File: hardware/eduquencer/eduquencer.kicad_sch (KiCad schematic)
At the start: 5 parts, among them J1 AudioJack2_SwitchT, J2 AudioJack2_SwitchT, U1 Pico

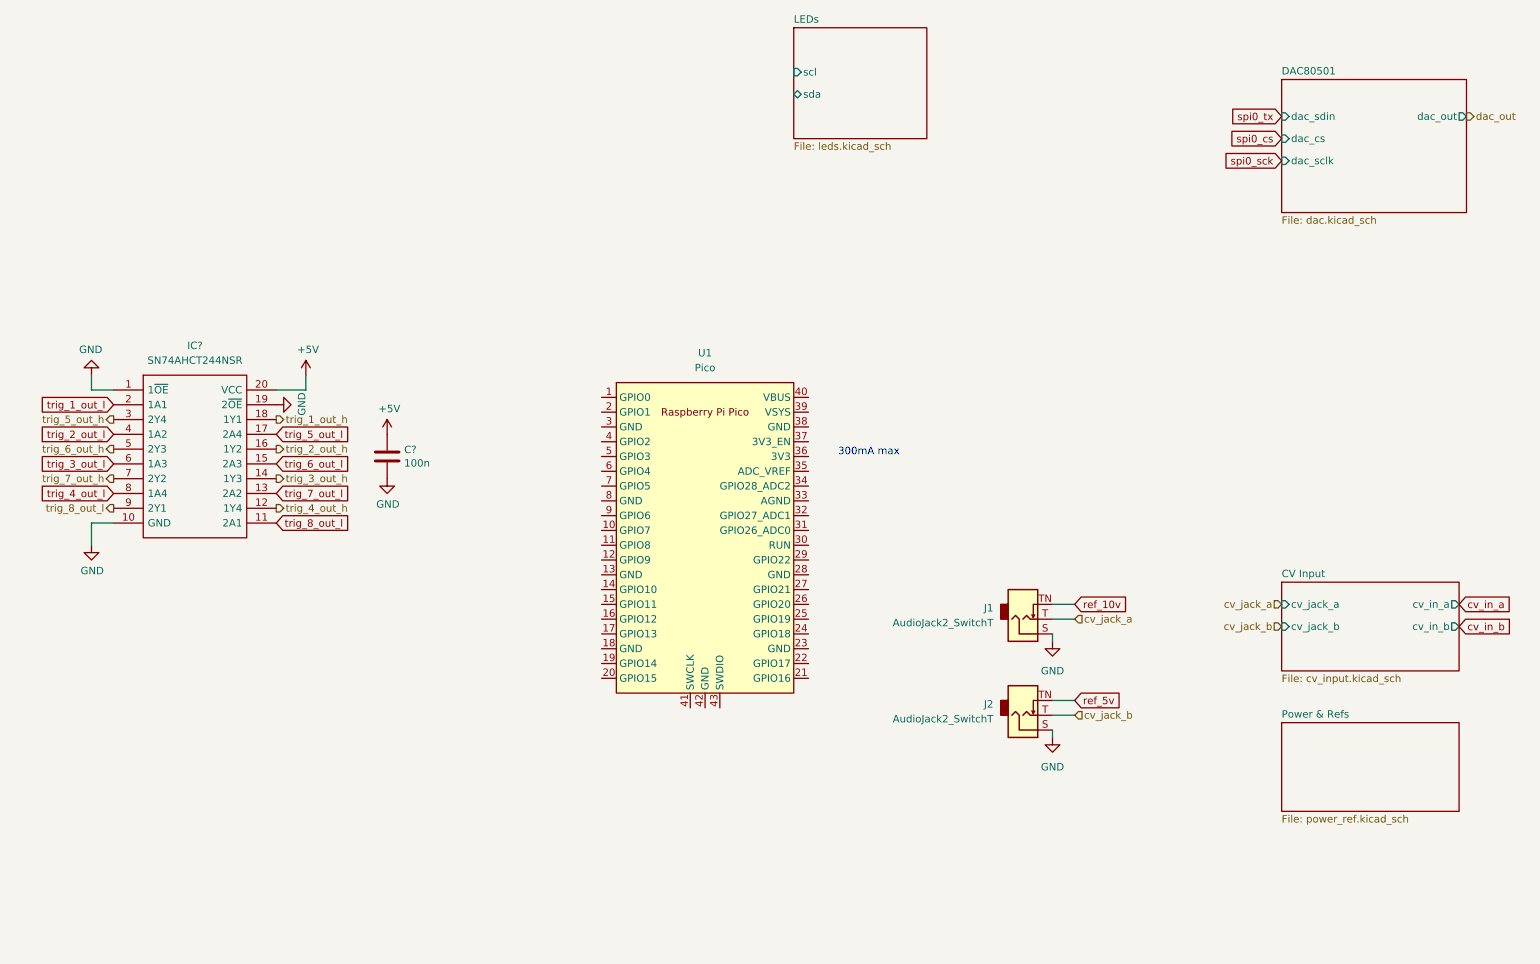
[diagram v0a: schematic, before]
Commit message: Hardware: add button sheet
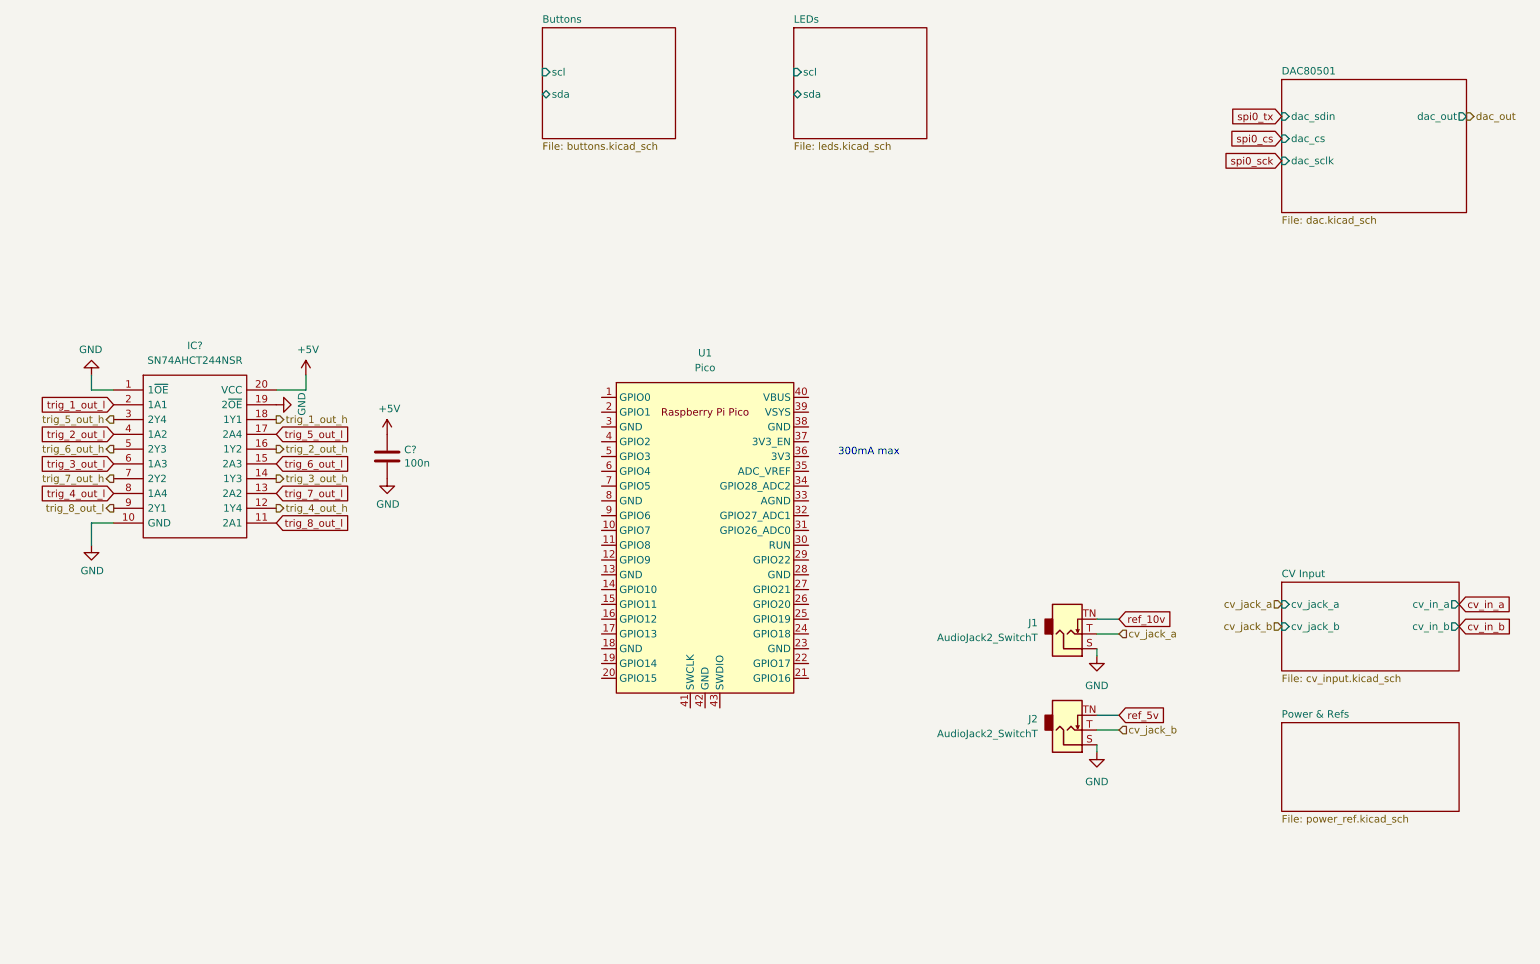
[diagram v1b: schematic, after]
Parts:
- J1, J2: footprint (none) -> AudioJacks:Jack_3.5mm_QingPu_WQP-PJ301BM_Vertical
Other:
- added sheet Buttons (buttons.kicad_sch)
- moved on the sheet: J1, J2

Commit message: Hardware: add trigger in&outputs, wire rpi
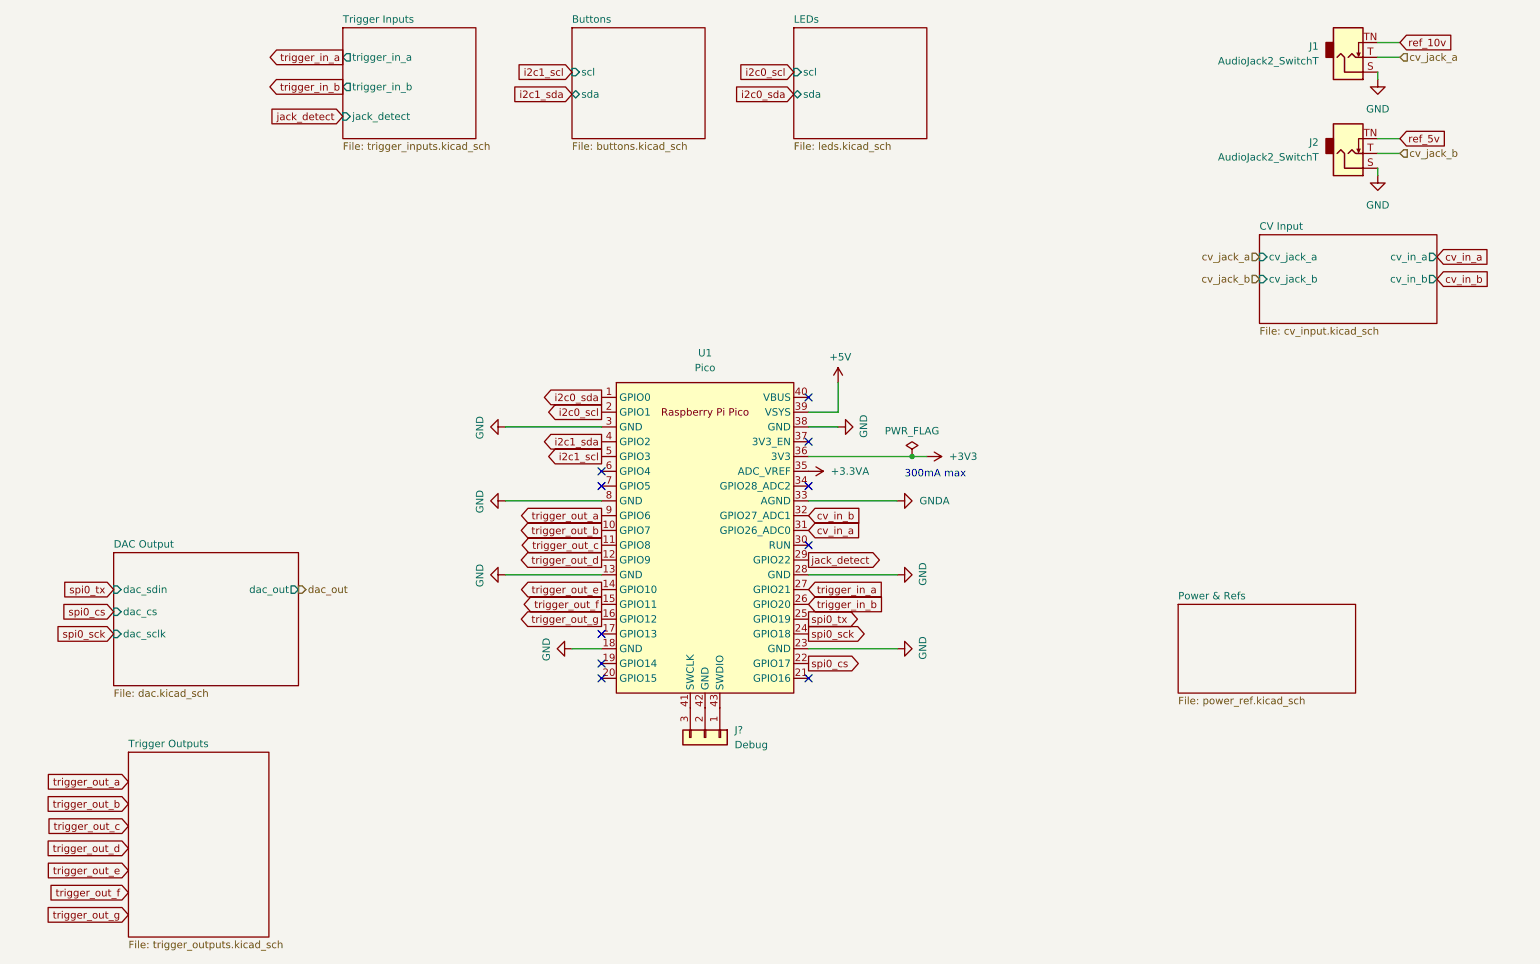
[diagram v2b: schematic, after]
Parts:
- removed C?: 100n, Capacitor_SMD:C_0603_1608Metric, symbol Device:C
- removed IC?: SN74AHCT244NSR, SOIC127P780X200-20N, symbol SN74AHCT244NSR:SN74AHCT244NSR
- added J?: Debug, symbol Connector_Generic:Conn_01x03
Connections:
- net +5V: now also U1.39 (VSYS)
- net GND: now also U1.13 (GND), U1.18 (GND), U1.23 (GND), U1.28 (GND), U1.3 (GND), U1.38 (GND), U1.8 (GND)
- net cv_in_a: now also U1.31 (GPIO26_ADC0)
- net cv_in_b: now also U1.32 (GPIO27_ADC1)
- net spi0_cs: now also U1.22 (GPIO17)
- net spi0_sck: now also U1.24 (GPIO18)
- net spi0_tx: now also U1.25 (GPIO19)
- net i2c0_sda: now reaches U1.1 (GPIO0)
- net trigger_out_b: now reaches U1.10 (GPIO7)
- net trigger_out_c: now reaches U1.11 (GPIO8)
- net trigger_out_d: now reaches U1.12 (GPIO9)
- net trigger_out_e: now reaches U1.14 (GPIO10)
- net trigger_out_f: now reaches U1.15 (GPIO11)
- net trigger_out_g: now reaches U1.16 (GPIO12)
- net i2c0_scl: now reaches U1.2 (GPIO1)
- net trigger_in_b: now reaches U1.26 (GPIO20)
- net trigger_in_a: now reaches U1.27 (GPIO21)
- net jack_detect: now reaches U1.29 (GPIO22)
- net GNDA: now reaches U1.33 (AGND)
- net +3.3VA: now reaches U1.35 (ADC_VREF)
- net +3V3: now reaches U1.36 (3V3)
- net i2c1_sda: now reaches U1.4 (GPIO2)
- net at U1.41 (SWCLK): now also J?.3 (Pin_3)
- net at U1.42 (GND): now also J?.2 (Pin_2)
- net at U1.43 (SWDIO): now also J?.1 (Pin_1)
- net i2c1_scl: now reaches U1.5 (GPIO3)
- net trigger_out_a: now reaches U1.9 (GPIO6)
- no-connect marks 0 -> 10
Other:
- sheet DAC80501 renamed DAC Output
- added sheet Trigger Inputs (trigger_inputs.kicad_sch)
- added sheet Trigger Outputs (trigger_outputs.kicad_sch)
- moved on the sheet: J1, J2

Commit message: Hardware: add test points, tiny cleanup
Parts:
- removed J1, J2: AudioJack2_SwitchT, AudioJacks:Jack_3.5mm_QingPu_WQP-PJ301BM_Vertical, symbol Connector:AudioJack2_SwitchT
- added TP?: SPI0 TX, TestPoint:TestPoint_Pad_2.0x2.0mm, symbol Connector:TestPoint
- added TP?: SPI0 CS, TestPoint:TestPoint_Pad_2.0x2.0mm, symbol Connector:TestPoint
- added TP?: I2C0 SDA, TestPoint:TestPoint_Pad_2.0x2.0mm, symbol Connector:TestPoint
- added TP?: I2C1 SCL, TestPoint:TestPoint_Pad_2.0x2.0mm, symbol Connector:TestPoint
- added TP?: I2C1 SDA, TestPoint:TestPoint_Pad_2.0x2.0mm, symbol Connector:TestPoint
- added TP?: SPI0 SCK, TestPoint:TestPoint_Pad_2.0x2.0mm, symbol Connector:TestPoint
- added TP?: I2C0 SCL, TestPoint:TestPoint_Pad_2.0x2.0mm, symbol Connector:TestPoint
- J?: footprint (none) -> Connector_PinHeader_2.54mm:PinHeader_1x03_P2.54mm_Vertical
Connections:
- net i2c0_scl: now also TP?.1
- net i2c0_sda: now also TP?.1
- net i2c1_scl: now also TP?.1
- net i2c1_sda: now also TP?.1
- net spi0_cs: now also TP?.1
- net spi0_sck: now also TP?.1
- net spi0_tx: now also TP?.1
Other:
- sheet CV Input ports: added none; removed cv_jack_a, cv_jack_b
- sheet Trigger Outputs ports: added trig_out_a, trig_out_b, trig_out_c, trig_out_d, trig_out_e, trig_out_f, trig_out_g; removed none
- note added: "Test Points"
- moved on the sheet: J?, U1

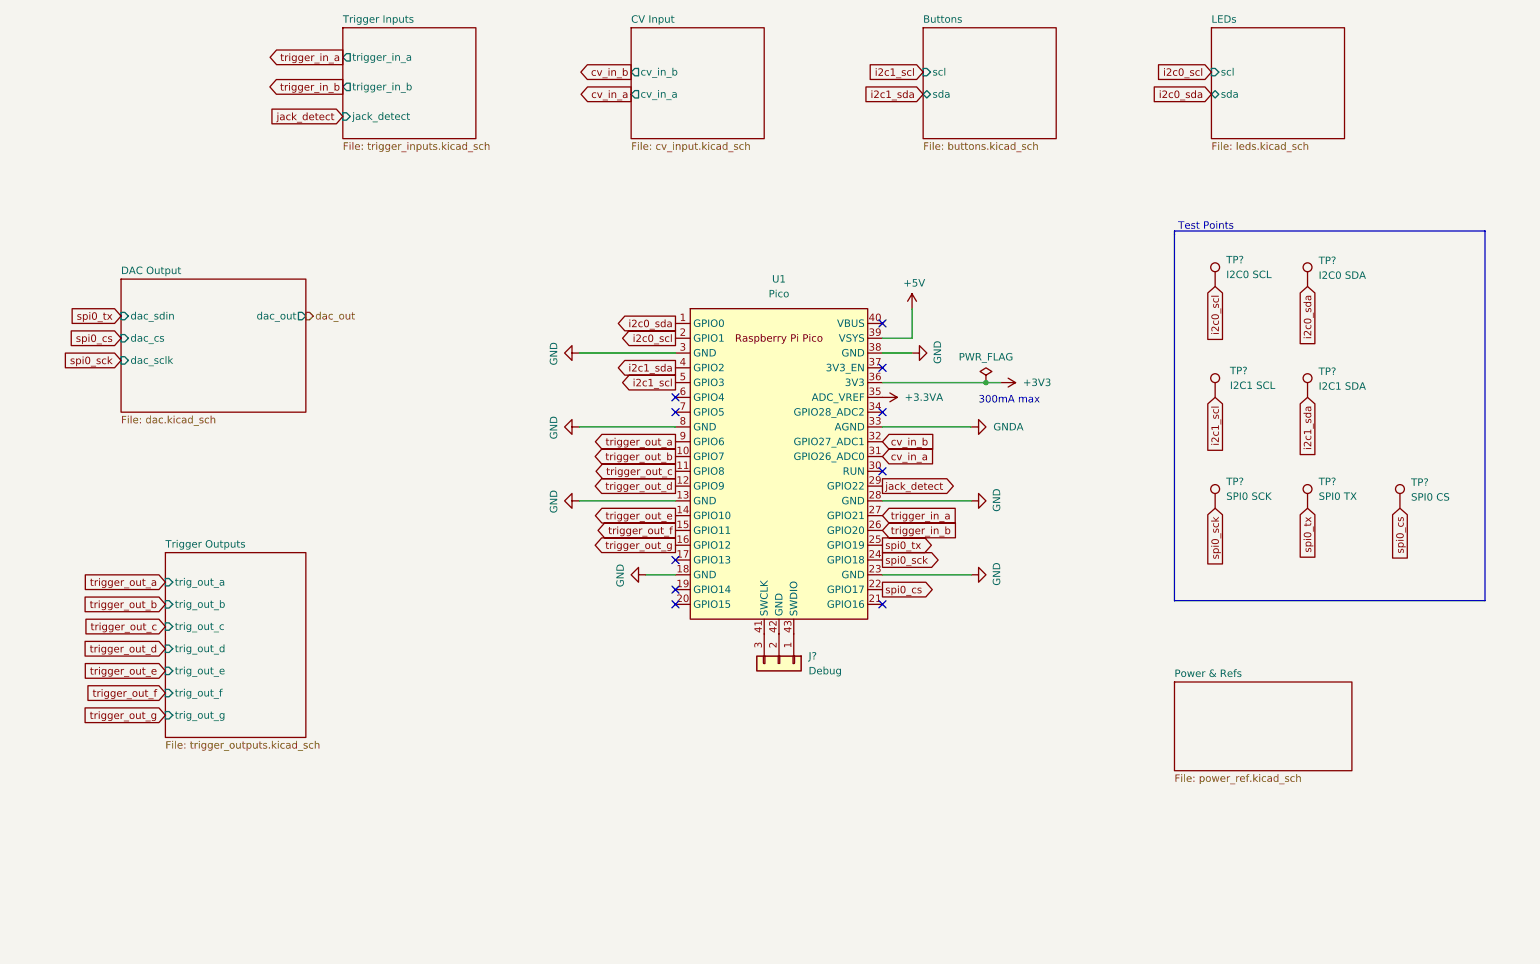
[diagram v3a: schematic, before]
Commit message: Hardware: update models, annotate, fix ERC issues
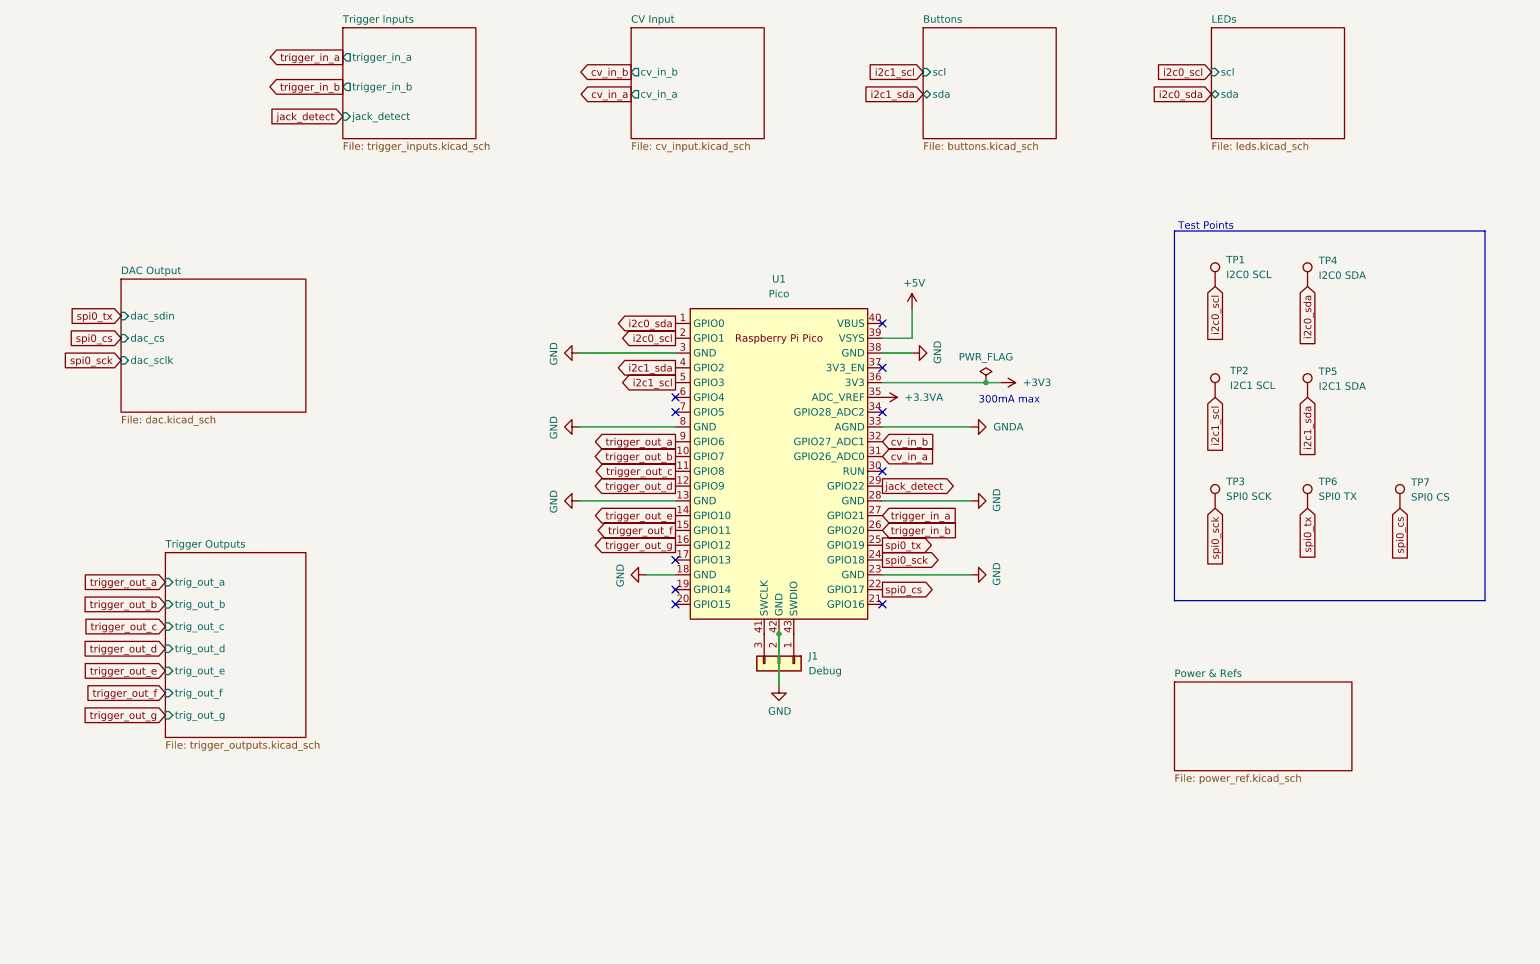
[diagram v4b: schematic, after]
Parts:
- gave numbers to parts that had none: 8
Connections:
- net GND: now also J1.2 (Pin_2), U1.42 (GND)
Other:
- sheet DAC Output ports: added none; removed dac_out
